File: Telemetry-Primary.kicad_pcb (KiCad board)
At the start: 2 copper layers, 95 x 82 mm, 152 parts, among them J1 CAN_LogicAnalyzer, J10 SMAConn, J11 CAN_In, J12 CAN_Out, J13 SWD, J2 IMU_LogicAnalyzer, J3 GPS_LogicAnalyzer, J4 SWD, J5 SDCard_LogicAnalyzer, J6 USB_B_Micro, J7 PowerConn, J8 RJ45_Abracon_ARJP11A-MASA-B-A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, J9 Micro_SD_Card_Det, SW1 Reset, SW2 RTCC_BattCheck, SW3 GPS_BattCheck, U1 STM32F429ZITx, U10 LAN8742A-CZ-TR, U11 USBLC6-4SC6, U2 RI3-1205S, U3 LD1117-3.3_SOT223, U4 ADM3055E, U5 CDSOT23-T24CAN, U6 BNO055, U7 MTK3339, U8 CP2102N-A02-GQFN24, U9 BLUENRG-M2SA, Y1 8M, Y2 25M, Y3 32.768k

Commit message: layout rearranging
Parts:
- removed J13: SWD, Connector_PinHeader_2.54mm:PinHeader_1x04_P2.54mm_Vertical
- added C60: 1u, Capacitor_SMD:C_0805_2012Metric, F.Cu at (48.0, 81.8)
- added C61: .1u, Capacitor_SMD:C_0805_2012Metric, F.Cu at (48.0, 84.8)
- added C62: 0.1u, Capacitor_SMD:C_0805_2012Metric, B.Cu at (163.6, 111.9)
- added C63: 10u, Capacitor_SMD:C_0805_2012Metric, B.Cu at (163.6, 114.9)
- added C64: 4.7u, Capacitor_SMD:C_0805_2012Metric, B.Cu at (115.9, 81.7)
- added D13: D_Zener, Diode_SMD:D_SOD-123F, F.Cu at (53.0, 82.0)
- added Q1: Q_PMOS_GSD, Package_TO_SOT_SMD:SuperSOT-3, F.Cu at (52.8, 85.9)
- added R32: 10, Resistor_SMD:R_0805_2012Metric, F.Cu at (48.0, 87.8)
- added SW4: SW_Push, UTSVT_Special:SW_SPST_B3SL-1002P, F.Cu at (198.8, 81.3)
- added SW5: SW_Push, UTSVT_Special:SW_SPST_B3SL-1002P, F.Cu at (198.8, 89.6)
- added SW6: SW_Push, UTSVT_Special:SW_SPST_B3SL-1002P, F.Cu at (198.8, 98.0)
- added SW7: SW_Push, UTSVT_Special:SW_SPST_B3SL-1002P, F.Cu at (198.8, 106.3)
- C40, C41, LOGO2, R24: moved to B.Cu
- moved U9 75.3 mm to (159.0, 119.4), turned to 180 degrees
- moved R31 71.3 mm to (148.5, 121.0), turned to 90 degrees
- moved C51 70.6 mm to (148.5, 117.0), turned to 90 degrees
- moved J10 34.1 mm to (119.5, 49.2)
- moved R26 24.4 mm to (164.3, 53.9), turned to -90 degrees
- moved SW2 22.4 mm to (133.0, 105.1), turned to 90 degrees
- moved J3 21.9 mm to (138.5, 66.9), turned to -90 degrees
- moved R4 20.7 mm to (159.0, 76.4)
- moved D3 19.7 mm to (163.6, 57.0), turned to 0 degrees
- moved J4 18.4 mm to (147.6, 76.7), turned to -90 degrees
- moved H4 18.3 mm to (163.1, 105.6)
- moved SW3 17.8 mm to (162.2, 63.1)
- moved C40 16.4 mm to (157.7, 76.9)
- moved U8 16.0 mm to (154.7, 77.3), turned to 90 degrees
- moved BT2 13.0 mm to (152.5, 53.4), turned to 180 degrees
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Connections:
- net /USART6_TX renamed /PG14
- J3 pad 2: /USART1_TX -> /USART2_TX
- J3 pad 3: /USART1_RX -> /USART2_RX
- J3 pad 4: /PA8 -> /PD7
- J3 pad 5: /PA11 -> /PG9
- J7 pad 1: +12V -> Net-(J7-Pin_1)
- R27 pad 1: /PA8 -> /PD7
- U1 pad 124: /USART6_RX -> /PG9
- U7 pad 10: /USART1_TX -> /USART2_TX
- U7 pad 13: /PA11 -> /PG9
- U7 pad 5: /PA8 -> /PD7
- U7 pad 9: /USART1_RX -> /USART2_RX
- U8 pad 20: /USART3_TX -> /USART1_TX
- U8 pad 21: /USART3_RX -> /USART1_RX
- U9 pad 10: /USART2_RX -> /USART3_RX
- U9 pad 11: /USART2_TX -> /USART3_TX
- U9 pad 12: /Bluetooth/SWCLK -> unconnected-(U9-DIO9-Pad12)
- U9 pad 13: /Bluetooth/SWDIO -> unconnected-(U9-DIO10-Pad13)
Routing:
- net +3.3V: track 349.8 -> 401.4 mm
- net /PA11: track 43.2 -> 0.00 mm, vias 2 -> 0
- net /PA8: track 40.1 -> 0.00 mm, vias 2 -> 0
- net /PG9: track 0.00 -> 35.0 mm
- net /SPI3_CS: track 0.00 -> 33.4 mm
- net /SPI3_CLK: track 0.00 -> 33.4 mm
- net /SPI3_MISO: track 0.00 -> 32.8 mm
- net /SPI3_MOSI: track 0.00 -> 30.4 mm
- net /PD0: track 0.00 -> 30.0 mm
- net /PD1: track 0.00 -> 28.8 mm
- net /PD7: track 0.00 -> 27.3 mm
- net /USART2_TX: track 0.00 -> 20.6 mm
- net GND: track 125.2 -> 105.0 mm, vias 36 -> 34
- net /USART2_RX: track 0.00 -> 20.0 mm
- net /USART1_TX: track 37.5 -> 21.3 mm, vias 2 -> 0
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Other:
- board text added: "D7"
- board text added: "G9"
- board text removed: "A11"
- board text removed: "A8"
- board text removed: "Jump if end of bus"

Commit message: breakout port
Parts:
- added J13: Breakouts, Connector_PinHeader_2.54mm:PinHeader_1x06_P2.54mm_Vertical, F.Cu at (162.8, 69.8)
- C60, C61: moved to B.Cu
- moved C61 49.4 mm to (97.2, 88.7), turned to 180 degrees
- moved C60 49.4 mm to (97.2, 85.7), turned to 180 degrees
- moved R32 17.3 mm to (58.8, 74.3)
- moved Q1 11.7 mm to (61.4, 78.0)
- moved SW4 10.2 mm to (189.6, 85.9)
- moved SW5 10.2 mm to (189.6, 94.2)
- moved SW6 10.2 mm to (189.6, 102.6)
- moved SW7 10.2 mm to (189.6, 110.9)
- moved D13 6.28 mm to (57.8, 78.0), turned to 90 degrees
- moved J3 2.76 mm to (139.9, 69.3)
- moved D5 2.01 mm to (157.6, 82.0)
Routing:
- net Net-(J10-In): track 0.00 -> 23.3 mm
- net +3.3V: track 401.4 -> 407.7 mm
- net +12V: track 18.3 -> 12.2 mm
- net /PD1: track 28.8 -> 25.0 mm
- net /PD0: track 30.0 -> 26.9 mm
- net /SPI3_MISO: track 32.8 -> 30.8 mm
- net /PG9: track 35.0 -> 36.7 mm
- net /PD7: track 27.3 -> 29.0 mm
- net Net-(J6-D-): track 8.40 -> 10.0 mm, vias 0 -> 2
- net Net-(J6-D+): track 7.53 -> 9.11 mm
- net /SPI3_MOSI: track 30.4 -> 28.9 mm
- net /SPI3_CS: track 33.4 -> 34.7 mm
- net /USART2_TX: track 20.6 -> 21.5 mm
- net Net-(J6-VBUS): track 7.76 -> 6.98 mm
- net /SPI3_CLK: track 33.4 -> 32.8 mm
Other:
- board text added: "D0"
- board text added: "D1"

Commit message: power protection layout
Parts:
- moved R32 18.0 mm to (76.7, 74.7)
- moved D13 15.8 mm to (73.6, 79.5), turned to 180 degrees
- moved Q1 11.9 mm to (73.1, 75.8), turned to 90 degrees
- moved J7 9.38 mm to (74.6, 68.6)
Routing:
- net +12V: track 12.2 -> 21.2 mm
- net Net-(D13-A): track 0.00 -> 7.09 mm
- net Net-(J7-Pin_1): track 0.00 -> 6.80 mm
- net GNDPWR: track 15.6 -> 20.2 mm
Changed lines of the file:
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@@
   )
   (footprint "UTSVT_Connectors:Molex_MicroFit3.0_1x2xP3.00mm_PolarizingPeg_Vertical" (layer "F.Cu")
-    (at 74.422 77.93 90)
+    (at 74.5752 68.556 90)
     (property "P/N" "43650-0227")
     (property "Sheetfile" "PowerDist.kicad_sch")
@@
     (property "ki_keywords" "connector")
     (attr through_hole)
-    (fp_text reference "J7" (at -5.4836 -0.3556 180) (layer "F.SilkS")
+    (fp_text reference "J7" (at 6.326 3.1488 180) (layer "F.SilkS")
         (effects (font (size 1 1) (thickness 0.15)))
     )
@@
   )
   (footprint "Diode_SMD:D_SOD-123F" (layer "F.Cu")
-    (at 57.8436 77.9628 90)
+    (at 73.6092 79.4512 180)
     (descr "D_SOD-123F")
     (tags "D_SOD-123F")
@@
     (property "ki_keywords" "diode")
     (attr smd)
-    (fp_text reference "D13" (at -0.127 -1.905 90) (layer "F.SilkS")
+    (fp_text reference "D13" (at 0 -2.0828) (layer "F.SilkS")
         (effects (font (size 1 1) (thickness 0.15)))
     )
-    (fp_text value "D_Zener" (at 0 2.1 90) (layer "F.Fab")
+    (fp_text value "D_Zener" (at 0 2.1) (layer "F.Fab")
         (effects (font (size 1 1) (thickness 0.15)))
     )
-    (fp_text user "${REFERENCE}" (at -0.127 -1.905 90) (layer "F.Fab")
+    (fp_text user "${REFERENCE}" (at -0.127 -1.905) (layer "F.Fab")
         (effects (font (size 1 1) (thickness 0.15)))
     )
@@
     (fp_line (start 1.4 0.9) (end -1.4 0.9)
       (stroke (width 0.1) (type solid)) (layer "F.Fab"))
-    (pad "1" smd roundrect (at -1.4 0 90) (size 1.1 1.1) (layers "F.Cu" "F.Paste" "F.Mask") (roundrect_rratio 0.2272727273)
+    (pad "1" smd roundrect (at -1.4 0 180) (size 1.1 1.1) (layers "F.Cu" "F.Paste" "F.Mask") (roundrect_rratio 0.2272727273)
       (net 4 "+12V") (pinfunction "K") (pintype "passive"))
-    (pad "2" smd roundrect (at 1.4 0 90) (size 1.1 1.1) (layers "F.Cu" "F.Paste" "F.Mask") (roundrect_rratio 0.2272727273)
+    (pad "2" smd roundrect (at 1.4 0 180) (size 1.1 1.1) (layers "F.Cu" "F.Paste" "F.Mask") (roundrect_rratio 0.2272727273)
       (net 234 "Net-(D13-A)") (pinfunction "A") (pintype "passive"))
     (model "${KICAD6_3DMODEL_DIR}/Diode_SMD.3dshapes/D_SOD-123F.wrl"
@@
   )
   (footprint "Resistor_SMD:R_0805_2012Metric" (layer "F.Cu")
-    (at 58.758 74.2544)
+    (at 76.708 74.7268)
     (descr "Resistor SMD 0805 (2012 Metric), square (rectangular) end terminal, IPC_7351 nominal, (Body size source: IPC-SM-782 page 72, https://www.pcb-3d.com/wordpress/wp-content/uploads/ipc-sm-782a_amendment_1_and_2.pdf), generated with kicad-footprint-generator")
     (tags "resistor")
@@
     (property "ki_keywords" "R res resistor")
     (attr smd)
-    (fp_text reference "R32" (at 0 -1.65) (layer "F.SilkS")
+    (fp_text reference "R32" (at 0.9652 2.4384 90) (layer "F.SilkS")
         (effects (font (size 1 1) (thickness 0.15)))
     )
@@
   )
   (footprint "Package_TO_SOT_SMD:SuperSOT-3" (layer "F.Cu")
-    (at 61.3996 77.9628)
+    (at 73.1012 75.8444 90)
     (descr "3-pin SuperSOT package https://www.fairchildsemi.com/package-drawings/MA/MA03B.pdf")
     (tags "SuperSOT-3 SSOT-3")
@@
     (property "ki_keywords" "transistor PMOS P-MOS P-MOSFET")
     (attr smd)
-    (fp_text reference "Q1" (at 0 -2.35) (layer "F.SilkS")
+    (fp_text reference "Q1" (at -0.9652 2.6416 90) (layer "F.SilkS")
         (effects (font (size 1 1) (thickness 0.15)))
     )
-    (fp_text value "Q_PMOS_GSD" (at 0 2.4) (layer "F.Fab")
+    (fp_text value "Q_PMOS_GSD" (at 0 2.4 90) (layer "F.Fab")
         (effects (font (size 1 1) (thickness 0.15)))
     )
-    (fp_text user "${REFERENCE}" (at 0 0 90) (layer "F.Fab")
+    (fp_text user "${REFERENCE}" (at 0 0) (layer "F.Fab")
         (effects (font (size 0.5 0.5) (thickness 0.075)))
     )
@@
     (fp_line (start 0.7 1.45) (end -0.7 1.45)
       (stroke (width 0.12) (type solid)) (layer "F.Fab"))
-    (pad "1" smd rect (at -1.1 -0.95) (size 1.4 1) (layers "F.Cu" "F.Paste" "F.Mask")
+    (pad "1" smd rect (at -1.1 -0.95 90) (size 1.4 1) (layers "F.Cu" "F.Paste" "F.Mask")
       (net 234 "Net-(D13-A)") (pinfunction "G") (pintype "input"))
-    (pad "2" smd rect (at -1.1 0.95) (size 1.4 1) (layers "F.Cu" "F.Paste" "F.Mask")
+    (pad "2" smd rect (at -1.1 0.95 90) (size 1.4 1) (layers "F.Cu" "F.Paste" "F.Mask")
       (net 4 "+12V") (pinfunction "S") (pintype "passive"))
-    (pad "3" smd rect (at 1.1 0) (size 1.4 1) (layers "F.Cu" "F.Paste" "F.Mask")
+    (pad "3" smd rect (at 1.1 0 90) (size 1.4 1) (layers "F.Cu" "F.Paste" "F.Mask")
       (net 235 "Net-(J7-Pin_1)") (pinfunction "D") (pintype "passive"))
     (model "${KICAD6_3DMODEL_DIR}/Package_TO_SOT_SMD.3dshapes/SuperSOT-3.wrl"
@@
   (gr_line (start 115.3668 29.1592) (end 123.6824 29.1592)
     (stroke (width 0.12) (type default)) (layer "F.SilkS"))
-  (gr_line (start 82.804 62.3316) (end 71.4756 62.3316)
+  (gr_line (start 81.026 60.5028) (end 71.2978 60.5028)
     (stroke (width 0.12) (type solid)) (layer "F.SilkS"))
   (gr_line (start 109.8804 70.866) (end 109.8804 59.436)
@@
   (gr_line (start 125.5268 73.8124) (end 125.5268 45.8724)
     (stroke (width 0.12) (type solid)) (layer "F.SilkS"))
-  (gr_line (start 82.793331 62.320931) (end 110.9472 90.4748)
+  (gr_line (start 81.011851 60.5028) (end 110.9472 90.438149)
     (stroke (width 0.12) (type solid)) (layer "F.SilkS"))
   (gr_line (start 115.3824 45.0244) (end 115.3824 29.1592)
@@
     (effects (font (size 1 1) (thickness 0.15)))
   )
-  (gr_text "H" (at 78.2828 61.2648) (layer "F.SilkS")
+  (gr_text "H" (at 78.1812 54.2036) (layer "F.SilkS")
     (effects (font (size 1 1) (thickness 0.15)))
   )
@@
     (effects (font (size 1 1) (thickness 0.15)))
   )
-  (gr_text "L" (at 73.8632 61.2648) (layer "F.SilkS")
+  (gr_text "L" (at 73.8632 54.102) (layer "F.SilkS")
     (effects (font (size 1 1) (thickness 0.15)))
   )
@@
     (effects (font (size 1 1) (thickness 0.15)))
   )
-  (gr_text "GNDPWR" (at 75.184 69.0372) (layer "F.SilkS")
+  (gr_text "GNDPWR" (at 83.7692 66.7512 -45) (layer "F.SilkS")
     (effects (font (size 1 1) (thickness 0.15)))
   )
@@
   (segment (start 102.616 75.692) (end 102.616 72.816128) (width 0.254) (layer "F.Cu") (net 2))
   (segment (start 102.616 75.692) (end 104.14 77.216) (width 0.254) (layer "F.Cu") (net 2))
+  (segment (start 79.6312 70.612) (end 80.264 70.612) (width 0.508) (layer "F.Cu") (net 3))
+  (segment (start 74.5752 65.556) (end 79.6312 70.612) (width 0.508) (layer "F.Cu") (net 3))
+  (segment (start 80.0608 74.7268) (end 80.264 74.93) (width 0.508) (layer "F.Cu") (net 3))
+  (segment (start 77.6205 74.7268) (end 80.0608 74.7268) (width 0.508) (layer "F.Cu") (net 3))
   (segment (start 80.264 74.93) (end 80.264 70.612) (width 0.508) (layer "F.Cu") (net 3))
-  (segment (start 74.422 74.93) (end 80.264 74.93) (width 0.508) (layer "B.Cu") (net 3))
   (segment (start 80.264 70.612) (end 81.026 71.374) (width 0.508) (layer "B.Cu") (net 3))
   (segment (start 81.026 71.374) (end 85.344 71.374) (width 0.508) (layer "B.Cu") (net 3))
+  (segment (start 74.0512 78.4932) (end 75.0092 79.4512) (width 0.508) (layer "F.Cu") (net 4))
+  (segment (start 75.0092 79.4512) (end 76.9904 77.47) (width 0.381) (layer "F.Cu") (net 4))
+  (segment (start 76.9904 77.47) (end 80.264 77.47) (width 0.381) (layer "F.Cu") (net 4))
+  (segment (start 74.0512 76.9444) (end 74.0512 78.4932) (width 0.508) (layer "F.Cu") (net 4))
   (segment (start 80.264 77.47) (end 80.4164 77.6224) (width 0.508) (layer "B.Cu") (net 4))
   (segment (start 80.4164 77.6224) (end 85.344 77.6224) (width 0.508) (layer "B.Cu") (net 4))
@@
   (segment (start 100.838 116.332) (end 101.62 115.55) (width 0.254) (layer "F.Cu") (net 217))
   (segment (start 99.822 116.332) (end 100.838 116.332) (width 0.254) (layer "F.Cu") (net 217))
+  (segment (start 73.2607 75.8349) (end 72.1512 76.9444) (width 0.381) (layer "F.Cu") (net 234))
+  (segment (start 72.1512 76.9444) (end 72.1512 79.3932) (width 0.508) (layer "F.Cu") (net 234))
+  (segment (start 72.1512 79.3932) (end 72.2092 79.4512) (width 0.508) (layer "F.Cu") (net 234))
+  (segment (start 75.7955 74.7268) (end 74.6874 75.8349) (width 0.381) (layer "F.Cu") (net 234))
+  (segment (start 74.6874 75.8349) (end 73.2607 75.8349) (width 0.381) (layer "F.Cu") (net 234))
+  (segment (start 74.5752 73.2704) (end 74.5752 68.556) (width 0.508) (layer "F.Cu") (net 235))
+  (segment (start 73.1012 74.7444) (end 74.5752 73.2704) (width 0.508) (layer "F.Cu") (net 235))
   (segment (start 79.151 51.816) (end 82.598 48.369) (width 0.254) (layer "F.Cu") (net 240))
   (segment (start 97.6528 52.1716) (end 97.6528 51.7472) (width 0.25) (layer "F.Cu") (net 240))
@@
         (xy 77.724 83.566)
         (xy 71.12 83.566)
-        (xy 71.17988 62.308567)
-        (xy 82.880063 62.348499)
+        (xy 71.189277 58.972613)
+        (xy 79.594092 59.001299)
       )
     )

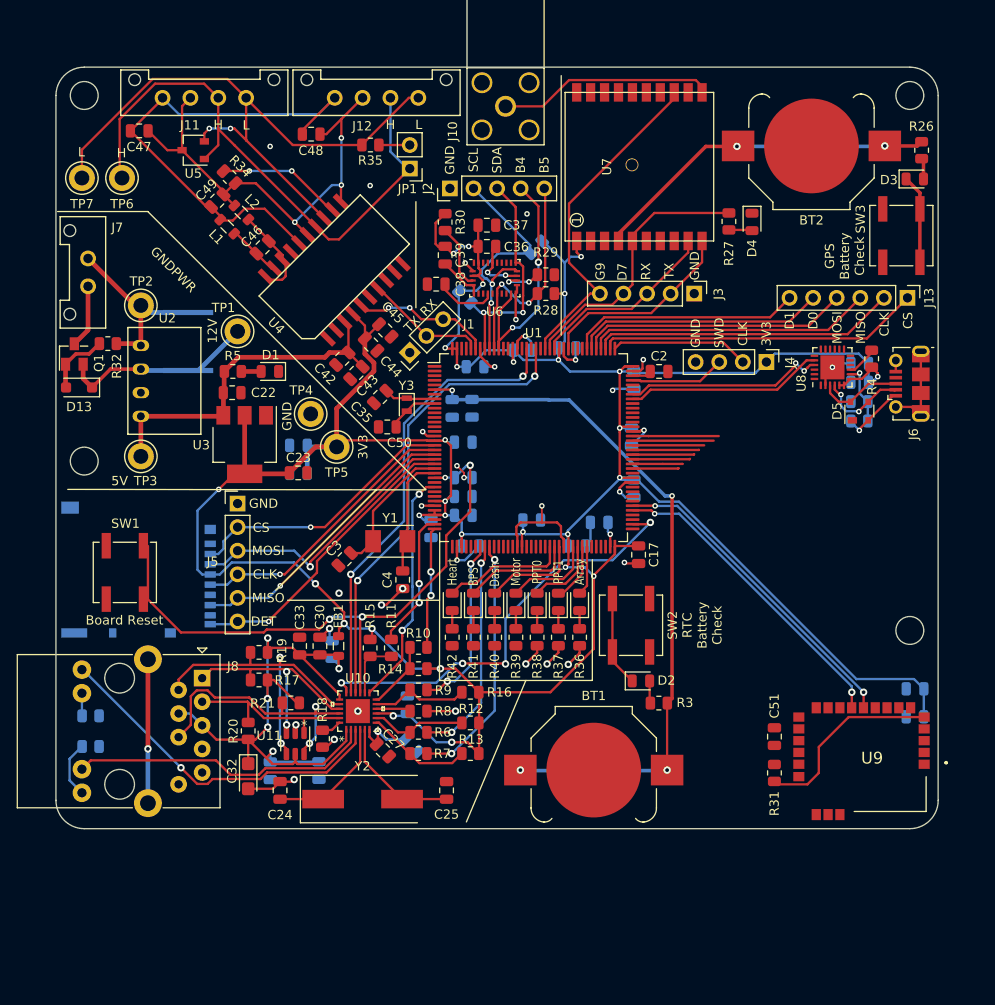
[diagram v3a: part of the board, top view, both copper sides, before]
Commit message: led fix + notes
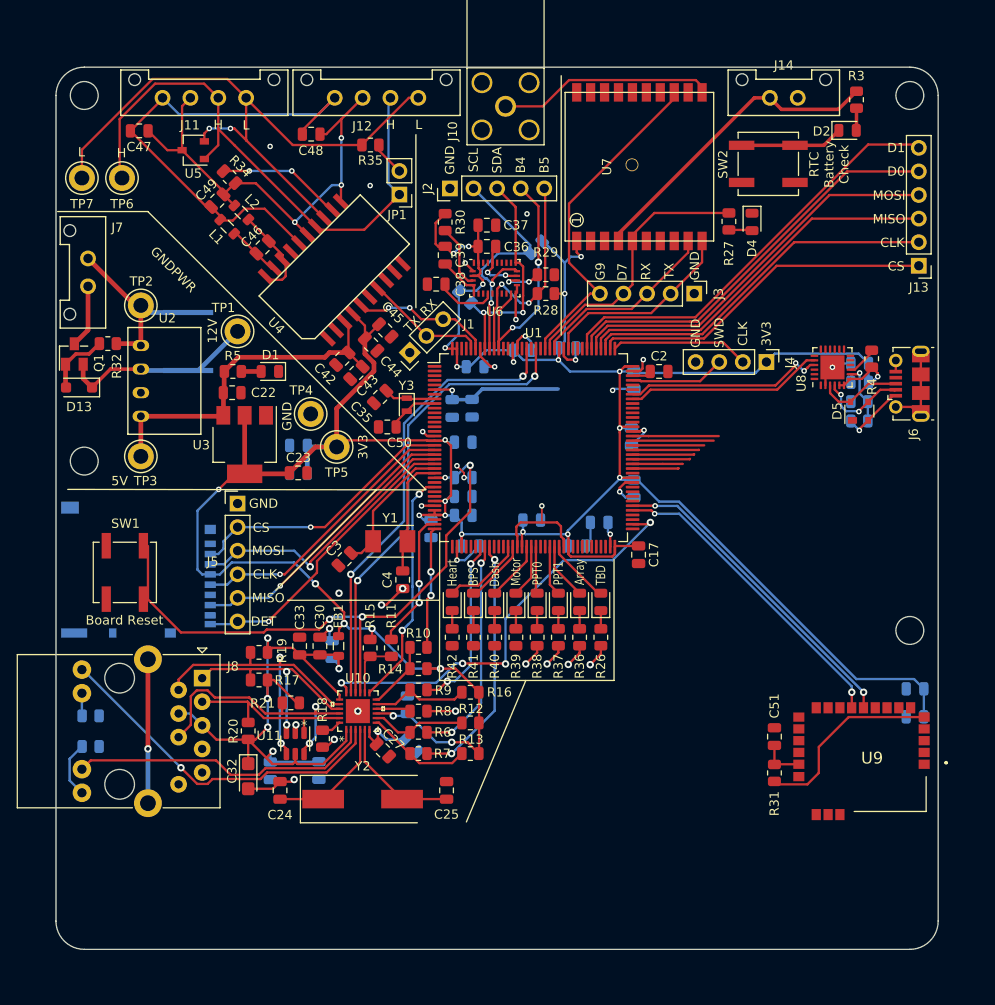
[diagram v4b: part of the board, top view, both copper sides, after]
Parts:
- removed BT1, BT2: CR1220, Battery:BatteryHolder_Keystone_3000_1x12mm
- removed the D2 at (134.1, 111.0)
- removed the R3 at (136.0, 113.4)
- removed the SW2 at (133.0, 105.1)
- added D3: RTDArray, LED_SMD:LED_0805_2012Metric, F.Cu at (129.8, 102.5)
- added J14: RTC_BATT, UTSVT_Connectors:Molex_MicroFit3.0_1x2xP3.00mm_PolarizingPeg_Vertical, F.Cu at (148.0, 48.3)
- added R26: 750, Resistor_SMD:R_0805_2012Metric, F.Cu at (129.8, 106.3)
- D2: renamed from D3; value GPS_BattCheck -> RTCC_BattCheck
- SW2: renamed from SW3; value GPS_BattCheck -> RTCC_BattCheck
- moved SW2 16.3 mm to (147.8, 55.4), turned to 0 degrees
- moved D2 8.93 mm to (156.4, 51.8)
- moved R3 8.87 mm to (157.3, 48.5)
- moved J13 3.66 mm to (164.0, 66.3), turned to 180 degrees
- moved JP1 3.01 mm to (108.1, 58.7)
- renumbered R26 to R3
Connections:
- net /PC6 renamed /USART6_TX
- net /PC7 renamed /USART7_TX
- D10 pad 2: /PE9 -> /PF13
- D11 pad 2: /PE8 -> /PF12
- D12 pad 2: /PE7 -> /PF11
- D6 pad 2: /PE13 -> /PE8
- D7 pad 2: /PE12 -> /PE7
- D8 pad 2: /PE11 -> /PF15
- D9 pad 2: /PE10 -> /PF14
- R3 pad 1: /GPS/GPS_VBAT -> +BATT
- U7 pad 4: /GPS/GPS_VBAT -> +BATT
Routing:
- net /GPS/GPS_VBAT: track 37.7 -> 0.00 mm, vias 2 -> 0
- net +BATT: track 76.5 -> 48.6 mm, vias 4 -> 1
- net +3.3V: track 407.7 -> 382.4 mm, vias 29 -> 27
- net /PD1: track 25.0 -> 45.9 mm
- net /PD0: track 26.9 -> 43.9 mm
- net /SPI3_MOSI: track 28.9 -> 42.3 mm
- net /SPI3_MISO: track 30.8 -> 40.7 mm
- net Net-(D2-K) (its old number): track 9.75 -> 0.00 mm
- net /PE10: track 9.64 -> 0.00 mm
- net /PF11: track 0.00 -> 8.67 mm
- net /PE7: track 13.6 -> 5.39 mm
- net /PE11: track 8.01 -> 0.00 mm
- net /PF12: track 0.00 -> 6.96 mm
- net /PF13: track 0.00 -> 6.43 mm
- net /PE12: track 6.38 -> 0.00 mm
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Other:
- board size 95 x 82 mm -> 95 x 95 mm
- board text added: "TBD"
- board text removed: "GPS Battery Check"
